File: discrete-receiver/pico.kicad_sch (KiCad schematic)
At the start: 41 parts, among them U6 RP2350A, U7 W25Q128, X2 X322512MSB4SI

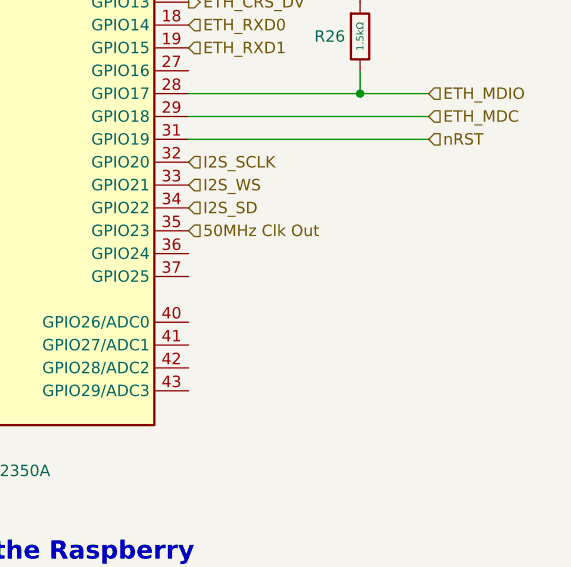
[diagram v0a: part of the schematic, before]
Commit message: Added a note about ethernet clocking
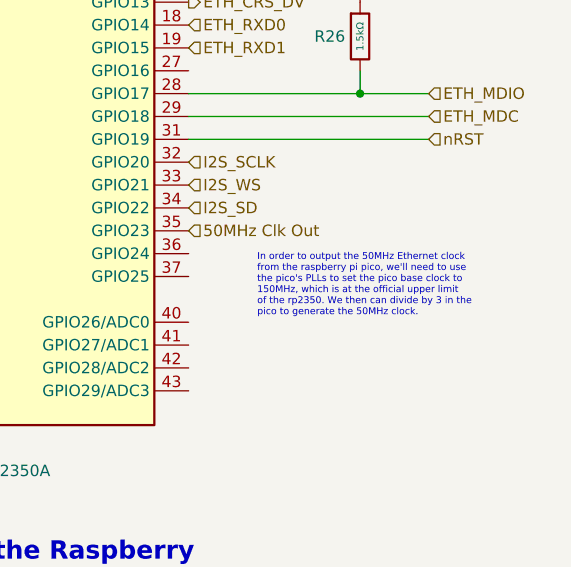
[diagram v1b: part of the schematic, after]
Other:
- note added: "In order to output the 50MHz Ethernet clock from the raspberry pi pico, we'll need to use the pico's PLLs to set the pico base clock to 150MHz, which is at the official upper limit of the rp2350. We then can divide by 3 in the pico to generate the 50MHz clock."
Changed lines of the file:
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@@
+		)
+	)
+	(text "In order to output the 50MHz Ethernet clock\nfrom the raspberry pi pico, we'll need to use\nthe pico's PLLs to set the pico base clock to\n150MHz, which is at the official upper limit\nof the rp2350. We then can divide by 3 in the\npico to generate the 50MHz clock."
+		(exclude_from_sim no)
+		(at 254 139.446 0)
+		(effects
+			(font
+				(size 0.762 0.762)
+				(thickness 0.0953)
+			)
+			(justify left)
 		)
 	)

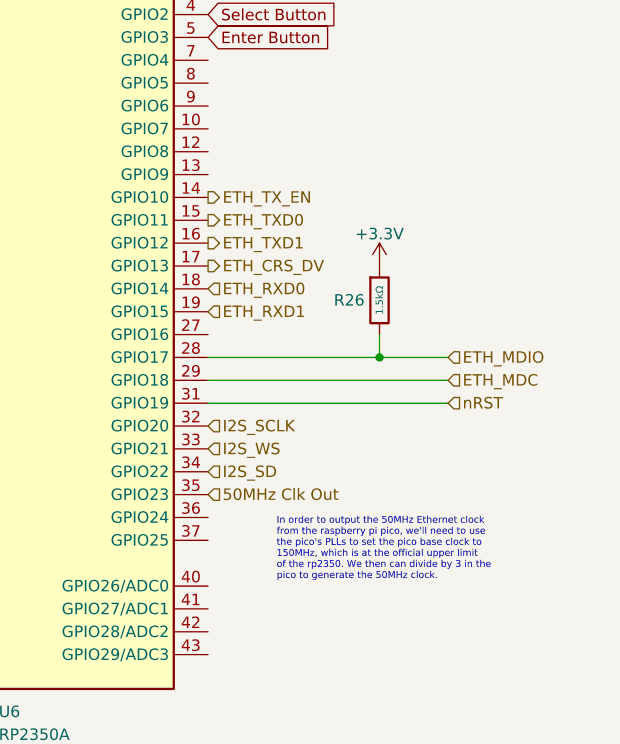
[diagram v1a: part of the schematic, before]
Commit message: Made schematic updates
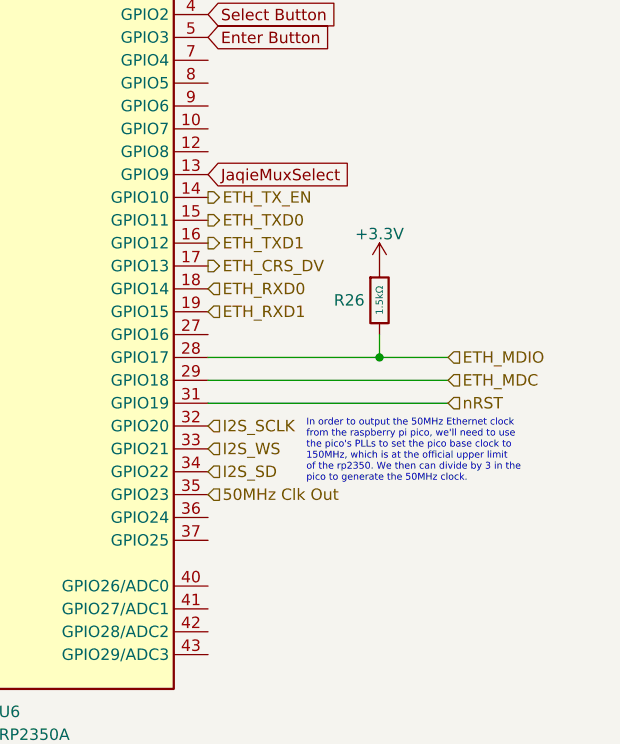
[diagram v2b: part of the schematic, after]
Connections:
- net JaqieMuxSelect: now reaches U6.13 (GPIO9)
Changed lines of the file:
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@@
 	(text "In order to output the 50MHz Ethernet clock\nfrom the raspberry pi pico, we'll need to use\nthe pico's PLLs to set the pico base clock to\n150MHz, which is at the official upper limit\nof the rp2350. We then can divide by 3 in the\npico to generate the 50MHz clock."
 		(exclude_from_sim no)
-		(at 254 139.446 0)
+		(at 257.302 128.524 0)
 		(effects
 			(font
@@
 			(hide yes)
 			(show_name no)
+			(do_not_autoplace no)
+			(effects
+				(font
+					(size 1.27 1.27)
+				)
+				(justify left)
+			)
+		)
+	)
+	(global_label "JaqieMuxSelect"
+		(shape input)
+		(at 246.38 97.79 0)
+		(fields_autoplaced yes)
+		(effects
+			(font
+				(size 1.27 1.27)
+			)
+			(justify left)
+		)
+		(property "Intersheetrefs" "${INTERSHEET_REFS}"
+			(at 263.8189 97.79 0)
+			(hide yes)
+			(show_name no)

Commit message: Updated schematic
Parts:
- removed C14, C17: 15pF, symbol Device:C_Small
- added C14, C17: 33pF, PCM_JLCPCB:C_0402, symbol PCM_JLCPCB-Capacitors:0402,33pF
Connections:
- net GND: now also C14.1, C17.1
- net XIN: now also C14.2
- net at R5.1, X2.1: now also C17.2
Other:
- note removed: "CHANGE CAP VALUES!!!!"
- moved on the sheet: X2

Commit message: 😢
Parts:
- removed R10: 0Ω, PCM_JLCPCB:R_0402, symbol PCM_JLCPCB-Resistors:0402,0Ω
- added R2: 1kΩ, PCM_JLCPCB:R_0402, symbol PCM_JLCPCB-Resistors:0402,1kΩ
- added R22: 10kΩ, PCM_JLCPCB:R_0402, symbol PCM_JLCPCB-Resistors:0402,10kΩ
- added S4: Tactile Button, 160gf, PCM_JLCPCB:SW_TS-1088-AR02016, symbol PCM_JLCPCB-Connectors_Buttons:Tactile Button, 160gf, 12V, 50mA, 4.0mm
- L1: LCSC (none) -> C42411119
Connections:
- net +3.3V: now also R22.1
- net GND: now also S4.1 (A)
- net QSPI_SS: now also R11.2, R12.1, U7.1 (~{CS}), R2.2
- new net Boot: R2.1, R22.2, S4.2 (B)
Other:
- note added: "Boot Button"
- note added: "WTF?? Polarized??"
- note removed: "NOT JLC'D!!!!"

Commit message: :)
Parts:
- C13, C19, C21: Manufacturer Samsung Electro-Mechanics -> (none); Price 0.004USD -> (none)
- C14, C17: Manufacturer FH(Guangdong Fenghua Advanced Tech) -> (none); Price 0.004USD -> (none)
- C15, C16, C18, C20, C22, C23, C24, C25, C26, C27, C28, C29, C30, C31: Manufacturer Samsung Electro-Mechanics -> (none); Price 0.008USD -> (none)
- D1: Manufacturer Hubei KENTO Elec -> (none); Price 0.009USD -> (none)
- R13, R16, R17, R2, R22, R23, R24, R26, R5, R6, R7, R8, R9: Manufacturer UNI-ROYAL(Uniroyal Elec) -> (none); Price 0.004USD -> (none)
- S1, S2, S3, S4: Manufacturer XUNPU -> (none); Price 0.044USD -> (none)
- U7: Manufacturer Winbond Elec -> (none); Price 0.896USD -> (none)
- X2: Manufacturer Yangxing Tech -> (none); Price 0.068USD -> (none)

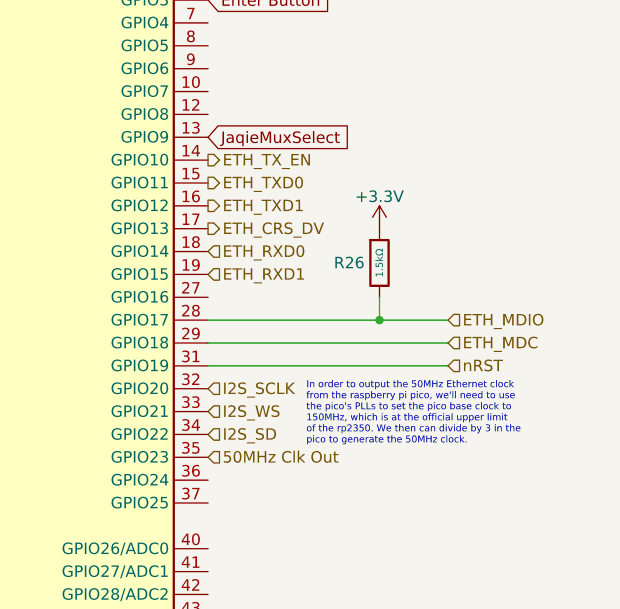
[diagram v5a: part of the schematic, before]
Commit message: Updated rp2350 GPIO mapping
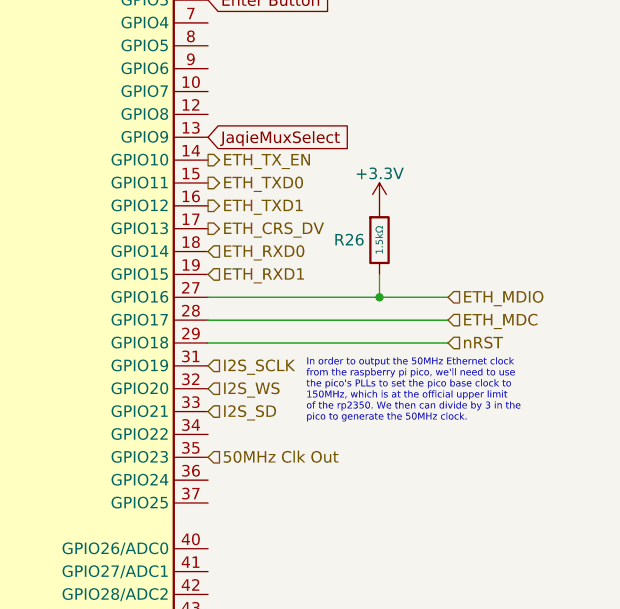
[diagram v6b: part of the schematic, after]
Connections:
- net ETH_MDC: now also U6.28 (GPIO17); no longer U6.29 (GPIO18)
- net ETH_MDIO: now also U6.27 (GPIO16); no longer U6.28 (GPIO17)
- net I2S_SCLK: now also U6.31 (GPIO19); no longer U6.32 (GPIO20)
- net I2S_SD: now also U6.33 (GPIO21); no longer U6.34 (GPIO22)
- net I2S_WS: now also U6.32 (GPIO20); no longer U6.33 (GPIO21)
- net nRST: now also U6.29 (GPIO18); no longer U6.31 (GPIO19)

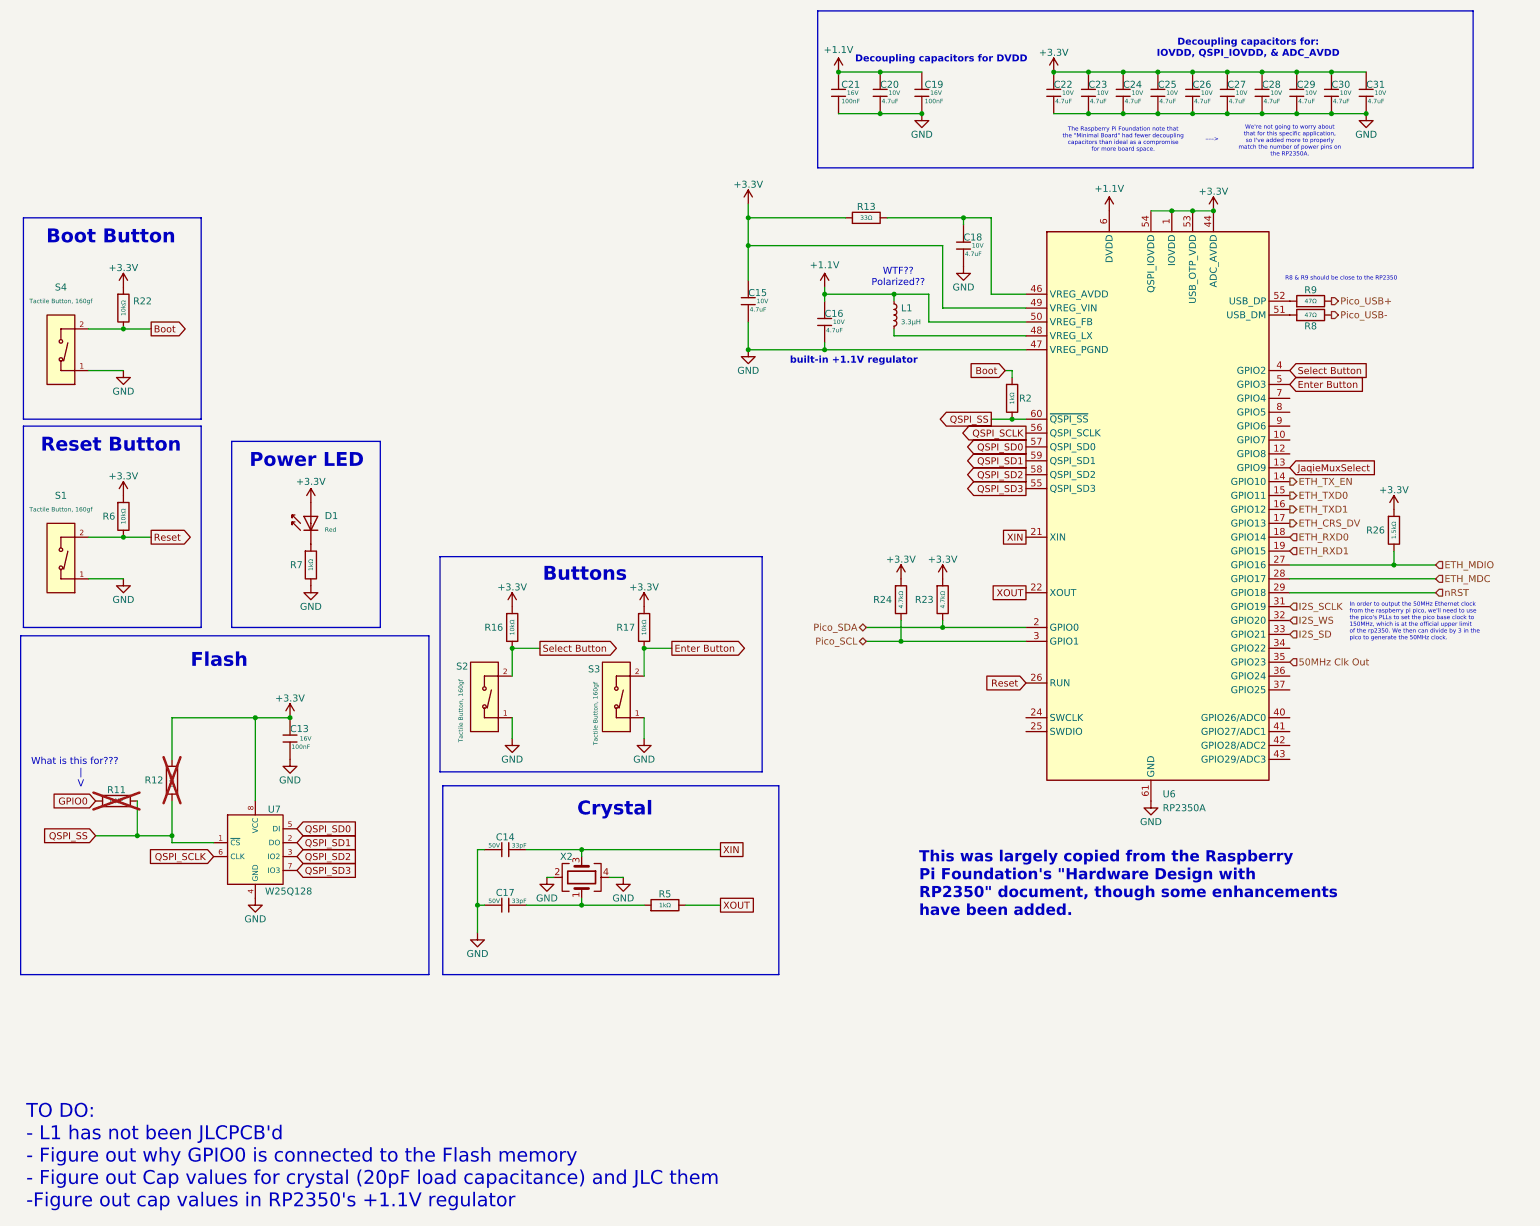
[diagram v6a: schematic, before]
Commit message: JLC'd L1
The inductor on the RP2350's +1.1V voltage regulator has been JLC'd with JLCPCB part information and a footprint.
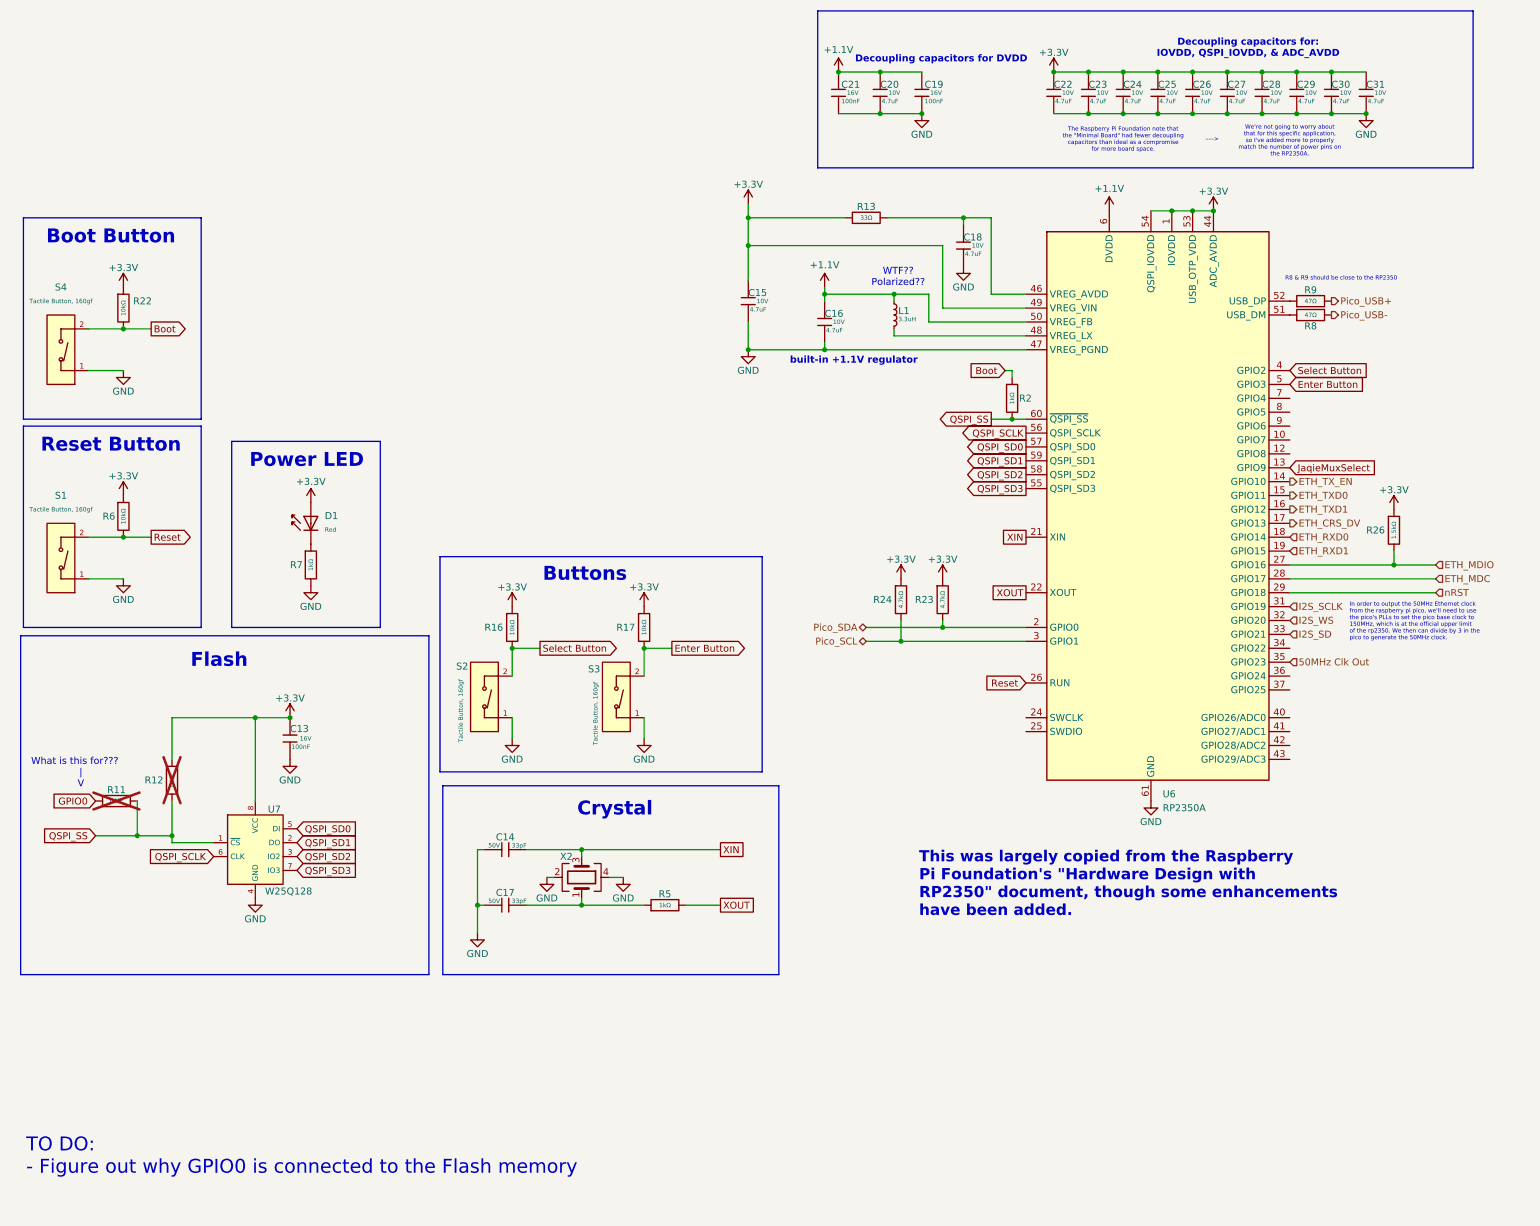
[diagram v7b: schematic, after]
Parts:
- removed L1: 3.3µH, symbol Device:L_Small
- added L1: 3.3uH, EasyEDA_Lib:IND-SMD_L2.0-W1.6_AOTA-B201610S3R3-101-T, symbol EasyEDA_Lib:AOTA-B201610S3R3-101-T
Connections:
- net +1.1V: now also L1.1
- net at U6.48 (VREG_LX): now also L1.2
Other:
- note added: "TO DO: - Figure out why GPIO0 is connected to the Flash memory"
- note removed: "TO DO: - L1 has not been JLCPCB'd - Figure out why GPIO0 is connected to the Flash memory - Figure out Cap values for crystal (20pF load capacitance) and JLC them -Figure out cap values in RP2350's +1.1V regulator"
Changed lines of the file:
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@@
 		)
 	)
-	(text "TO DO:\n- L1 has not been JLCPCB'd\n- Figure out why GPIO0 is connected to the Flash memory\n- Figure out Cap values for crystal (20pF load capacitance) and JLC them\n-Figure out cap values in RP2350's +1.1V regulator"
+	(text "TO DO:\n- Figure out why GPIO0 is connected to the Flash memory"
 		(exclude_from_sim no)
 		(at 15.24 223.774 0)
@@
 	)
 	(symbol
-		(lib_id "Device:L_Small")
-		(at 173.99 69.85 0)
-		(unit 1)
-		(body_style 1)
-		(exclude_from_sim no)
-		(in_bom yes)
-		(on_board yes)
-		(in_pos_files yes)
-		(dnp no)
-		(fields_autoplaced yes)
-		(property "Reference" "L1"
-			(at 175.26 68.5799 0)
-			(show_name no)
-			(do_not_autoplace no)
-			(effects
-				(font
-					(size 1.27 1.27)
-				)
-				(justify left)
-			)
-		)
-		(property "Value" "3.3µH"
-			(at 175.26 71.12 0)
-			(show_name no)
-			(do_not_autoplace no)
-			(effects
-				(font
-					(size 0.889 0.889)
-				)
-				(justify left)
-			)
-		)
-		(property "Footprint" ""
-			(at 173.99 69.85 0)
-			(hide yes)
-			(show_name no)
-			(do_not_autoplace no)
-			(effects
-				(font
-					(size 1.27 1.27)
-				)
-			)
-		)
-		(property "Datasheet" ""
-			(at 173.99 69.85 0)
-			(hide yes)
-			(show_name no)
-			(do_not_autoplace no)
-			(effects
-				(font
-					(size 1.27 1.27)
-				)
-			)
-		)
-		(property "Description" "Inductor, small symbol"
-			(at 173.99 69.85 0)
-			(hide yes)
-			(show_name no)
-			(do_not_autoplace no)
-			(effects
-				(font
-					(size 1.27 1.27)
-				)
-			)
-		)
-		(property "LCSC" "C42411119"
-			(at 173.99 69.85 0)
-			(hide yes)
-			(show_name no)
-			(do_not_autoplace no)
-			(effects
-				(font
-					(size 1.27 1.27)
-				)
-			)
-		)
-		(pin "1"
-		)
-		(pin "2"
-		)
-		(instances
-			(project "diode_tayloe_sdr"
-				(path "/d18d178d-3f10-4d68-9036-eae71a7d091a/55c641a1-b41f-4dd2-8726-b4449cdad787"
-					(reference "L1")
-					(unit 1)
-				)
-			)
-		)
-	)
-	(symbol
 		(lib_id "PCM_JLCPCB-Capacitors:0402,4.7uF")
 		(at 222.25 29.21 0)
@@
 					(unit 1)
 				)
+			)
+		)
+	)
+	(symbol
+		(lib_id "EasyEDA_Lib:AOTA-B201610S3R3-101-T")
+		(at 173.99 69.85 270)
+		(unit 1)
+		(body_style 1)
+		(exclude_from_sim no)
+		(in_bom yes)
+		(on_board yes)
+		(in_pos_files yes)
+		(dnp no)
+		(property "Reference" "L1"
+			(at 174.752 69.088 90)
+			(show_name no)
+			(do_not_autoplace no)
+			(effects
+				(font
+					(size 1.27 1.27)
+				)
+				(justify left)
+			)
+		)
+		(property "Value" "3.3uH"
+			(at 174.752 70.612 90)
+			(show_name no)
+			(do_not_autoplace no)
+			(effects
+				(font
+					(size 0.8 0.8)
+				)
+				(justify left)
+			)
+		)
+		(property "Footprint" "EasyEDA_Lib:IND-SMD_L2.0-W1.6_AOTA-B201610S3R3-101-T"
+			(at 173.99 69.85 0)
+			(hide yes)
+			(show_name no)
+			(do_not_autoplace no)
+			(effects
+				(font
+					(size 1.27 1.27)
+				)
+			)
+		)
+		(property "Datasheet" "https://item.szlcsc.com/datasheet/AOTA-B201610S3R3-101-T/44392932.html"
+			(at 173.99 69.85 0)
+			(hide yes)
+			(show_name no)
+			(do_not_autoplace no)
+			(effects
+				(font
+					(size 1.27 1.27)
+				)
+			)
+		)
+		(property "Description" "Inductance:3.3uH Current Rating:2.1A Current - Saturation(Isat):2.4A DC Resistance(DCR):115mΩ Type:Molded Inductor"
+			(at 173.99 69.85 0)
+			(hide yes)
+			(show_name no)
+			(do_not_autoplace no)
+			(effects
+				(font
+					(size 1.27 1.27)
+				)
+			)
+		)
+		(property "Manufacturer Part" "AOTA-B201610S3R3-101-T"
+			(at 173.99 69.85 0)
+			(hide yes)
+			(show_name no)
+			(do_not_autoplace no)
+			(effects
+				(font
+					(size 1.27 1.27)
+				)
+			)
+		)
+		(property "Manufacturer" "ABRACON"
+			(at 173.99 69.85 0)
+			(hide yes)
+			(show_name no)
+			(do_not_autoplace no)
+			(effects
+				(font
+					(size 1.27 1.27)
+				)
+			)
+		)
+		(property "Supplier Part" "C42411119"
+			(at 173.99 69.85 0)
+			(hide yes)
+			(show_name no)
+			(do_not_autoplace no)
+			(effects
+				(font
+					(size 1.27 1.27)
+				)
+			)
+		)
+		(property "Supplier" "LCSC"
+			(at 173.99 69.85 0)
+			(hide yes)
+			(show_name no)
+			(do_not_autoplace no)
+			(effects
+				(font
+					(size 1.27 1.27)
+				)
+			)
+		)
+		(property "LCSC Part Name" "3.3uH 2.4A"
+			(at 173.99 69.85 0)
+			(hide yes)
+			(show_name no)
+			(do_not_autoplace no)
+			(effects
+				(font
+					(size 1.27 1.27)
+				)
+			)
+		)
+		(pin "2"
+		)
+		(pin "1"
+		)
+		(instances
+			(project "diode_tayloe_sdr"
+				(path "/d18d178d-3f10-4d68-9036-eae71a7d091a/55c641a1-b41f-4dd2-8726-b4449cdad787"
+					(reference "L1")
+					(unit 1)
+				)

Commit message: Progress made on schematic
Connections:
- net VHF BP Filter Mux Select: now reaches U6.12 (GPIO8)
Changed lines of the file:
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@@
+		)
+	)
+	(global_label "VHF BP Filter Mux Select"
+		(shape input)
+		(at 246.38 95.25 0)
+		(fields_autoplaced yes)
+		(effects
+			(font
+				(size 1.27 1.27)
+			)
+			(justify left)
+		)
+		(property "Intersheetrefs" "${INTERSHEET_REFS}"
+			(at 273.7371 95.25 0)
+			(hide yes)
+			(show_name no)
+			(do_not_autoplace no)
+			(effects
+				(font
+					(size 1.27 1.27)
+				)
+				(justify left)
+			)
 		)
 	)
